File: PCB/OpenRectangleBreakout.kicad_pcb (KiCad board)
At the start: 2 copper layers, 46 parts, among them J1 USB C Connector, J2 JTAG_TC2030, J3 Conn_01x04_Pin, J4 Conn_01x04_Pin, J5 Conn_01x06_Pin, SW1 Boot, U1 XC6206, U2 USBLC6-2SC6, U3 RP2040, U4 W25Q128JVS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

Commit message: First version
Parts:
- removed REF**: PinHeader_1x05_P2.54mm_Vertical, Connector_PinHeader_2.54mm:PinHeader_1x05_P2.54mm_Vertical
- removed REF** (x2): PinHeader_1x08_P2.54mm_Vertical, Connector_PinHeader_2.54mm:PinHeader_1x08_P2.54mm_Vertical
- added H1: MountingHole_Pad, MountingHole:MountingHole_2.2mm_M2_ISO14580_Pad, F.Cu at (23.0, 31.8)
- added H2: MountingHole, MountingHole:MountingHole_2.1mm, F.Cu at (23.0, 85.8)
- added H3: MountingHole, MountingHole:MountingHole_2.1mm, F.Cu at (67.0, 85.8)
- added H4: MountingHole, MountingHole:MountingHole_2.1mm, F.Cu at (67.0, 31.8)
- added J6: Screw_Terminal_01x09, Connector_PinHeader_2.54mm:PinHeader_1x09_P2.54mm_Vertical, F.Cu at (23.0, 55.3)
- added J7: Screw_Terminal_01x09, Connector_PinHeader_2.54mm:PinHeader_1x09_P2.54mm_Vertical, F.Cu at (34.6, 85.8)
- added J8: Screw_Terminal_01x09, Connector_PinHeader_2.54mm:PinHeader_1x09_P2.54mm_Vertical, F.Cu at (67.0, 55.3)
- J5: value Conn_01x06_Pin -> GCC Cable; footprint Connector_PinHeader_2.54mm:PinHeader_1x06_P2.54mm_Vertical -> Connector_PinHeader_2.00mm:PinHeader_1x06_P2.00mm_Vertical
- R5, R6: footprint Resistor_SMD:R_0603_1608Metric -> Resistor_SMD:R_0402_1005Metric
- moved R2 140.3 mm to (41.3, 40.0), turned to 0 degrees
- moved R1 137.3 mm to (23.0, 35.8), turned to 90 degrees
- moved R3 135.3 mm to (46.1, 39.9), turned to -90 degrees
- moved C3 102.1 mm to (36.2, 44.9)
- moved J5 102.0 mm to (66.6, 40.2)
- moved R10 97.7 mm to (27.0, 42.9)
- moved U4 97.7 mm to (30.6, 46.8)
- moved SW1 97.4 mm to (31.5, 35.3)
- moved J1 97.3 mm to (45.0, 31.6)
- moved J3 97.3 mm to (52.6, 32.3)
- moved J4 97.3 mm to (37.4, 32.3)
- moved C10 97.1 mm to (45.0, 55.4)
- moved D2 97.1 mm to (55.2, 46.0)
- moved R4 97.1 mm to (54.7, 62.0)
- moved U2 97.1 mm to (45.0, 45.8)
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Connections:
- net Net-(J1-SHIELD) renamed Earth
- U3 pad 11: unconnected-(U3-GPIO8-Pad11) -> 8
- U3 pad 12: unconnected-(U3-GPIO9-Pad12) -> 9
- U3 pad 13: unconnected-(U3-GPIO10-Pad13) -> 10
- U3 pad 14: unconnected-(U3-GPIO11-Pad14) -> 11
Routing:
- net DATA: track 22.7 -> 68.6 mm, vias 1 -> 3
- net Earth: track 0.00 -> 40.7 mm
- net 11: track 0.00 -> 34.5 mm, vias 0 -> 1
- net 10: track 0.00 -> 33.5 mm, vias 0 -> 1
- net 3vCable: track 8.80 -> 41.9 mm, vias 0 -> 1
- net 9: track 0.00 -> 33.1 mm, vias 0 -> 1
- net VCC: track 10.1 -> 37.7 mm, vias 2 -> 3
- net 8: track 0.00 -> 26.5 mm
- net Net-(J1-CC2): track 0.00 -> 22.8 mm, vias 0 -> 1
- net CS: track 6.14 -> 28.3 mm
- net SD1: track 6.63 -> 25.4 mm
- net A: track 16.0 -> 32.2 mm, vias 0 -> 1
- net C_UP: track 17.3 -> 32.8 mm, vias 0 -> 1
- net SD2: track 7.12 -> 21.6 mm
- net C_RT: track 17.0 -> 30.1 mm
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- added copper zone on B.Cu, net GND
- added copper zone on F.Cu, net GND
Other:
- board outline added: 50 x 60 mm
- board text added: "D3V"
- board text added: "GND"
- board text added: "GND C DN C LT A C UP C RT GP9 SEL HOME"
- board text added: "GND L LEFT DOWN RIGHT MX MY START GP8"
- board text added: "GND R B Y X LS Z MS UP"

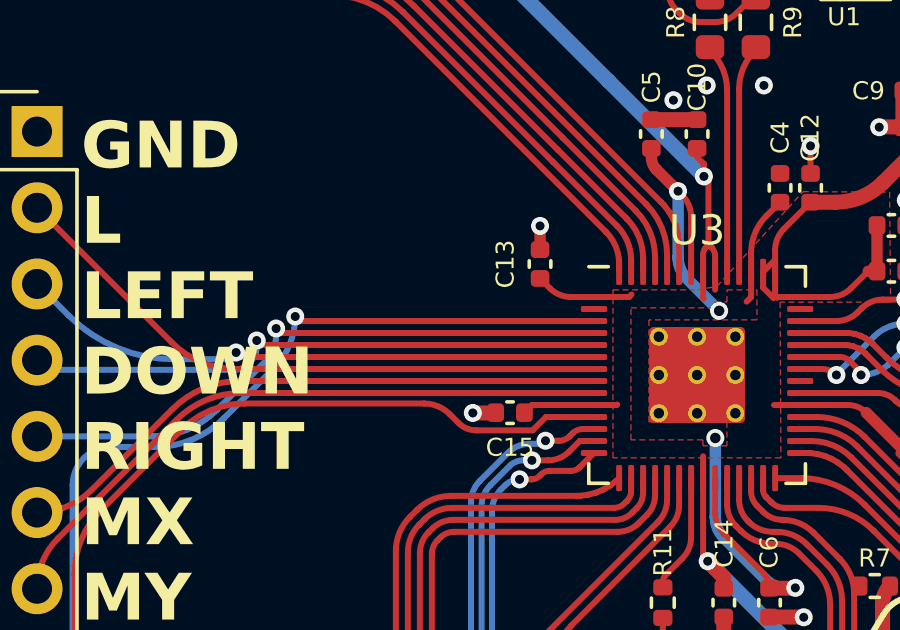
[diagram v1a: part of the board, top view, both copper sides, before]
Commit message: Fixed START button to the correct pin
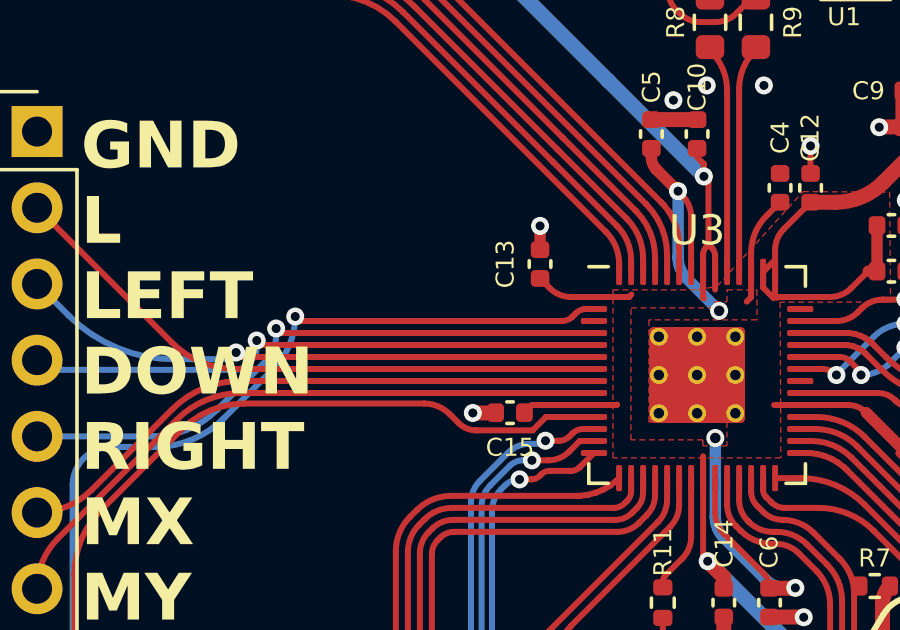
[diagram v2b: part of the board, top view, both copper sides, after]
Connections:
- net 10 renamed SELECT
- net 11 renamed HOME
- U3 pad 2: unconnected-(U3-GPIO0-Pad2) -> START
- U3 pad 3: START -> unconnected-(U3-GPIO1-Pad3)
